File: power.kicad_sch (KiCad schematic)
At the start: 21 parts, among them U4 AMS1117-3.3, U5 TPS562202

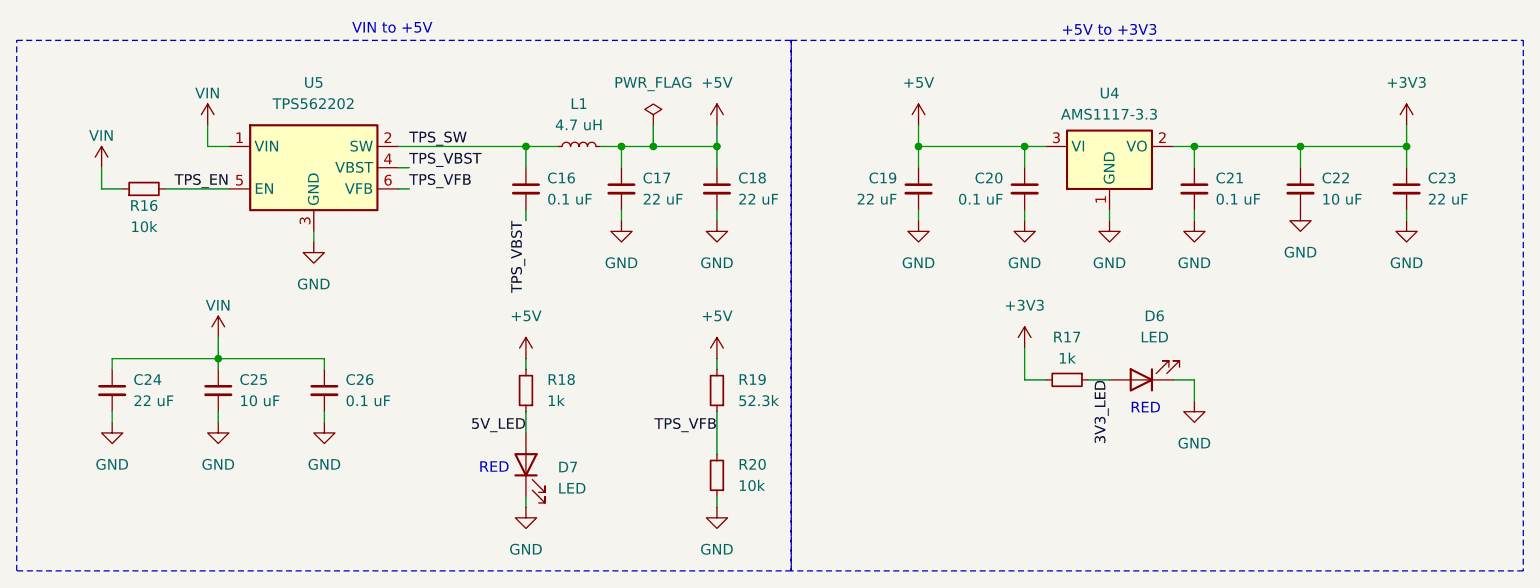
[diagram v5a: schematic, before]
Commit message: Added more graphics, removed some unnecessary features. moved GPU passive components upper. added switching components to LoRa.
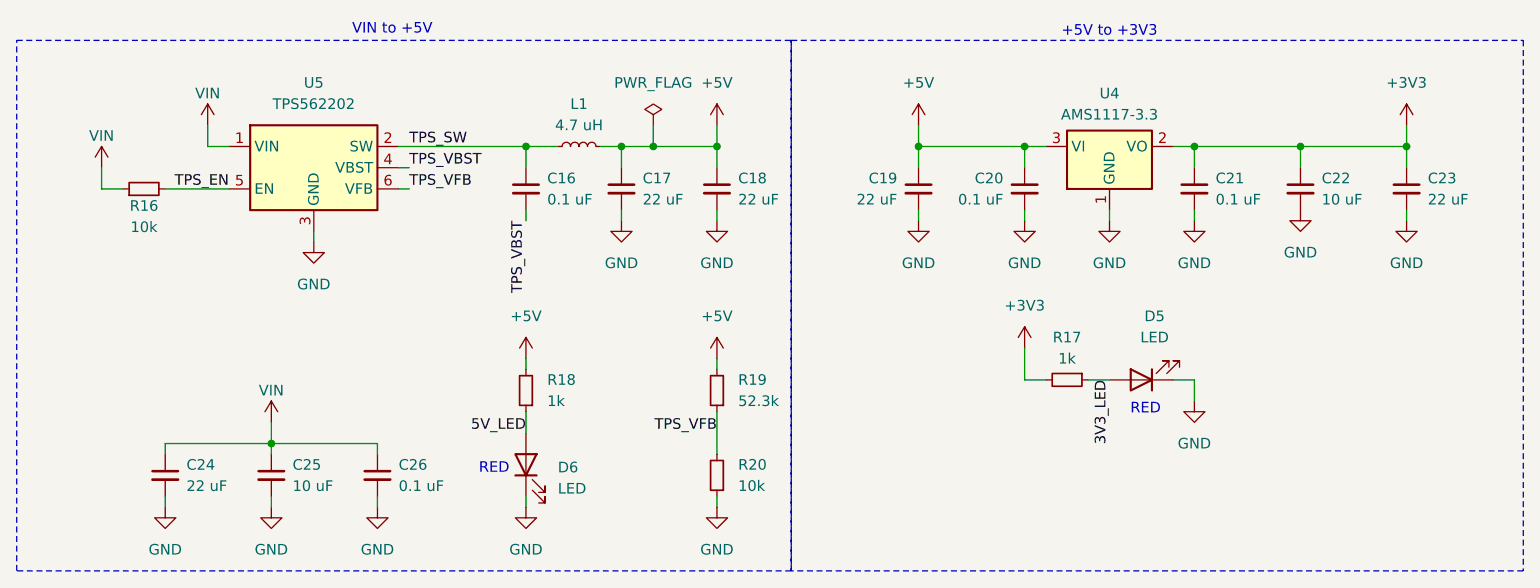
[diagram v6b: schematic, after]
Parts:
- renumbered D6 to D5, D7 to D6
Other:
- moved on the sheet: C24, C25, C26
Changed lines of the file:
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@@
 	)
 	(junction
-		(at 74.93 96.52)
+		(at 81.28 106.68)
 		(diameter 0)
 		(color 0 0 0 0)
@@
 	(wire
 		(pts
-			(xy 87.63 96.52) (xy 87.63 97.79)
+			(xy 93.98 106.68) (xy 93.98 107.95)
 		)
 		(stroke
@@
 	(wire
 		(pts
-			(xy 74.93 93.98) (xy 74.93 96.52)
+			(xy 81.28 104.14) (xy 81.28 106.68)
 		)
 		(stroke
@@
 	(wire
 		(pts
-			(xy 62.23 102.87) (xy 62.23 104.14)
+			(xy 68.58 113.03) (xy 68.58 114.3)
 		)
 		(stroke
@@
 	(wire
 		(pts
-			(xy 74.93 96.52) (xy 74.93 97.79)
+			(xy 81.28 106.68) (xy 81.28 107.95)
 		)
 		(stroke
@@
 	(wire
 		(pts
-			(xy 74.93 96.52) (xy 62.23 96.52)
+			(xy 81.28 106.68) (xy 68.58 106.68)
 		)
 		(stroke
@@
 	(wire
 		(pts
-			(xy 87.63 102.87) (xy 87.63 104.14)
+			(xy 93.98 113.03) (xy 93.98 114.3)
 		)
 		(stroke
@@
 	(wire
 		(pts
-			(xy 62.23 96.52) (xy 62.23 97.79)
+			(xy 68.58 106.68) (xy 68.58 107.95)
 		)
 		(stroke
@@
 	(wire
 		(pts
-			(xy 87.63 96.52) (xy 74.93 96.52)
+			(xy 93.98 106.68) (xy 81.28 106.68)
 		)
 		(stroke
@@
 	(wire
 		(pts
-			(xy 74.93 102.87) (xy 74.93 104.14)
+			(xy 81.28 113.03) (xy 81.28 114.3)
 		)
 		(stroke
@@
 		(dnp no)
 		(fields_autoplaced yes)
-		(property "Reference" "D7"
+		(property "Reference" "D6"
 			(at 115.57 109.5374 90)
 			(effects
@@
 			(project ""
 				(path "/d24fd15c-a242-4d26-9876-7755ca0d378c/739f0b15-c53d-4f01-9ae2-b7e797c20069"
-					(reference "D7")
+					(reference "D6")
 					(unit 1)
 				)
@@
 	(symbol
 		(lib_id "Device:C_Small")
-		(at 74.93 100.33 0)
+		(at 81.28 110.49 0)
 		(unit 1)
 		(exclude_from_sim no)
@@
 		(fields_autoplaced yes)
 		(property "Reference" "C25"
-			(at 77.47 99.0662 0)
+			(at 83.82 109.2262 0)
 			(effects
 				(font
@@
 		)
 		(property "Value" "10 uF"
-			(at 77.47 101.6062 0)
+			(at 83.82 111.7662 0)
 			(effects
 				(font
@@
 		)
 		(property "Footprint" "Capacitor_SMD:C_0805_2012Metric"
-			(at 74.93 100.33 0)
+			(at 81.28 110.49 0)
 			(effects
 				(font
@@
 		)
 		(property "Datasheet" "~"
-			(at 74.93 100.33 0)
+			(at 81.28 110.49 0)
 			(effects
 				(font
@@
 		)
 		(property "Description" "Unpolarized capacitor, small symbol"
-			(at 74.93 100.33 0)
+			(at 81.28 110.49 0)
 			(effects
 				(font
@@
 	(symbol
 		(lib_id "power:GND")
-		(at 74.93 104.14 0)
+		(at 81.28 114.3 0)
 		(unit 1)
 		(exclude_from_sim no)
@@
 		(fields_autoplaced yes)
 		(property "Reference" "#PWR061"
-			(at 74.93 110.49 0)
+			(at 81.28 120.65 0)
 			(effects
 				(font
@@
 		)
 		(property "Value" "GND"
-			(at 74.93 109.22 0)
+			(at 81.28 119.38 0)
 			(effects
 				(font
@@
 		)
 		(property "Footprint" ""
-			(at 74.93 104.14 0)
+			(at 81.28 114.3 0)
 			(effects
 				(font
@@
 		)
 		(property "Datasheet" ""
-			(at 74.93 104.14 0)
+			(at 81.28 114.3 0)
 			(effects
 				(font
@@
 		)
 		(property "Description" "Power symbol creates a global label with name \"GND\" , ground"
-			(at 74.93 104.14 0)
+			(at 81.28 114.3 0)
 			(effects
 				(font
@@
 	(symbol
 		(lib_id "power:GND")
-		(at 87.63 104.14 0)
+		(at 93.98 114.3 0)
 		(unit 1)
 		(exclude_from_sim no)
@@
 		(fields_autoplaced yes)
 		(property "Reference" "#PWR062"
-			(at 87.63 110.49 0)
+			(at 93.98 120.65 0)
 			(effects
 				(font
@@
 		)
 		(property "Value" "GND"
-			(at 87.63 109.22 0)
+			(at 93.98 119.38 0)
 			(effects
 				(font
@@
 		)
 		(property "Footprint" ""
-			(at 87.63 104.14 0)
+			(at 93.98 114.3 0)
 			(effects
 				(font
@@
 		)
 		(property "Datasheet" ""
-			(at 87.63 104.14 0)
+			(at 93.98 114.3 0)
 			(effects
 				(font
@@
 		)
 		(property "Description" "Power symbol creates a global label with name \"GND\" , ground"
-			(at 87.63 104.14 0)
+			(at 93.98 114.3 0)
 			(effects
 				(font
@@
 	(symbol
 		(lib_id "Device:C_Small")
-		(at 87.63 100.33 0)
+		(at 93.98 110.49 0)
 		(unit 1)
 		(exclude_from_sim no)
@@
 		(fields_autoplaced yes)
 		(property "Reference" "C26"
-			(at 90.17 99.0662 0)
+			(at 96.52 109.2262 0)
 			(effects
 				(font
@@
 		)
 		(property "Value" "0.1 uF"
-			(at 90.17 101.6062 0)
+			(at 96.52 111.7662 0)
 			(effects
 				(font
@@
 		)
 		(property "Footprint" "Capacitor_SMD:C_0805_2012Metric"
-			(at 87.63 100.33 0)
+			(at 93.98 110.49 0)
 			(effects
 				(font
@@
 		)
 		(property "Datasheet" "~"
-			(at 87.63 100.33 0)
+			(at 93.98 110.49 0)
 			(effects
 				(font
@@
 		)
 		(property "Description" "Unpolarized capacitor, small symbol"
-			(at 87.63 100.33 0)
+			(at 93.98 110.49 0)
 			(effects
 				(font
@@
 	(symbol
 		(lib_id "SparkFun-PowerSymbol:VIN")
-		(at 74.93 93.98 0)
+		(at 81.28 104.14 0)
 		(unit 1)
 		(exclude_from_sim no)
@@
 		(fields_autoplaced yes)
 		(property "Reference" "#PWR055"
-			(at 74.93 97.79 0)
+			(at 81.28 107.95 0)
 			(effects
 				(font
@@
 		)
 		(property "Value" "VIN"
-			(at 74.93 90.17 0)
+			(at 81.28 100.33 0)
 			(do_not_autoplace yes)
 			(effects
@@
 		)
 		(property "Footprint" ""
-			(at 74.93 93.98 0)
+			(at 81.28 104.14 0)
 			(effects
 				(font
@@
 		)
 		(property "Datasheet" ""
-			(at 74.93 93.98 0)
+			(at 81.28 104.14 0)
 			(effects
 				(font
@@
 		)
 		(property "Description" "Power symbol creates a global label with name \"VIN\""
-			(at 74.93 100.33 0)
+			(at 81.28 110.49 0)
 			(effects
 				(font
@@
 	(symbol
 		(lib_id "Device:C_Small")
-		(at 62.23 100.33 0)
+		(at 68.58 110.49 0)
 		(mirror y)
 		(unit 1)
@@
 		(dnp no)
 		(property "Reference" "C24"
-			(at 64.77 99.0662 0)
+			(at 71.12 109.2262 0)
 			(effects
 				(font
@@
 		)
 		(property "Value" "22 uF"
-			(at 64.77 101.6062 0)
+			(at 71.12 111.7662 0)
 			(effects
 				(font
@@
 		)
 		(property "Footprint" "Capacitor_SMD:C_0805_2012Metric"
-			(at 62.23 100.33 0)
+			(at 68.58 110.49 0)
 			(effects
 				(font
@@
 		)
 		(property "Datasheet" "~"
-			(at 62.23 100.33 0)
+			(at 68.58 110.49 0)
 			(effects
 				(font
@@
 		)
 		(property "Description" "Unpolarized capacitor, small symbol"
-			(at 62.23 100.33 0)
+			(at 68.58 110.49 0)
 			(effects
 				(font
@@
 		(on_board yes)
 		(dnp no)
-		(fields_autoplaced yes)
 		(property "Reference" "#PWR054"
 			(at 86.36 88.9 0)
@@
 	(symbol
 		(lib_id "power:GND")
-		(at 62.23 104.14 0)
+		(at 68.58 114.3 0)
 		(unit 1)
 		(exclude_from_sim no)
@@
 		(fields_autoplaced yes)
 		(property "Reference" "#PWR060"
-			(at 62.23 110.49 0)
+			(at 68.58 120.65 0)
 			(effects
 				(font
@@
 		)
 		(property "Value" "GND"
-			(at 62.23 109.22 0)
+			(at 68.58 119.38 0)
 			(effects
 				(font
@@
 		)
 		(property "Footprint" ""
-			(at 62.23 104.14 0)
+			(at 68.58 114.3 0)
 			(effects
 				(font
@@
 		)
 		(property "Datasheet" ""
-			(at 62.23 104.14 0)
+			(at 68.58 114.3 0)
 			(effects
 				(font
@@
 		)
 		(property "Description" "Power symbol creates a global label with name \"GND\" , ground"
-			(at 62.23 104.14 0)
+			(at 68.58 114.3 0)
 			(effects
 				(font
@@
 		(dnp no)
 		(fields_autoplaced yes)
-		(property "Reference" "D6"
+		(property "Reference" "D5"
 			(at 187.0075 91.44 0)
 			(effects
@@
 			(project "valkyriev3"
 				(path "/d24fd15c-a242-4d26-9876-7755ca0d378c/739f0b15-c53d-4f01-9ae2-b7e797c20069"
-					(reference "D6")
+					(reference "D5")
 					(unit 1)
 				)
